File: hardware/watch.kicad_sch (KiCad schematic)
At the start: 30 parts, among them J1 DEBUG, J2 RTC_CALIB, J3 RST, Q1 BC846, SW1 MODE, SW2 ALARM, SW3 LIGHT, U1 STM32L053C8Ux, U2 LCD, Y1 32.768kHz

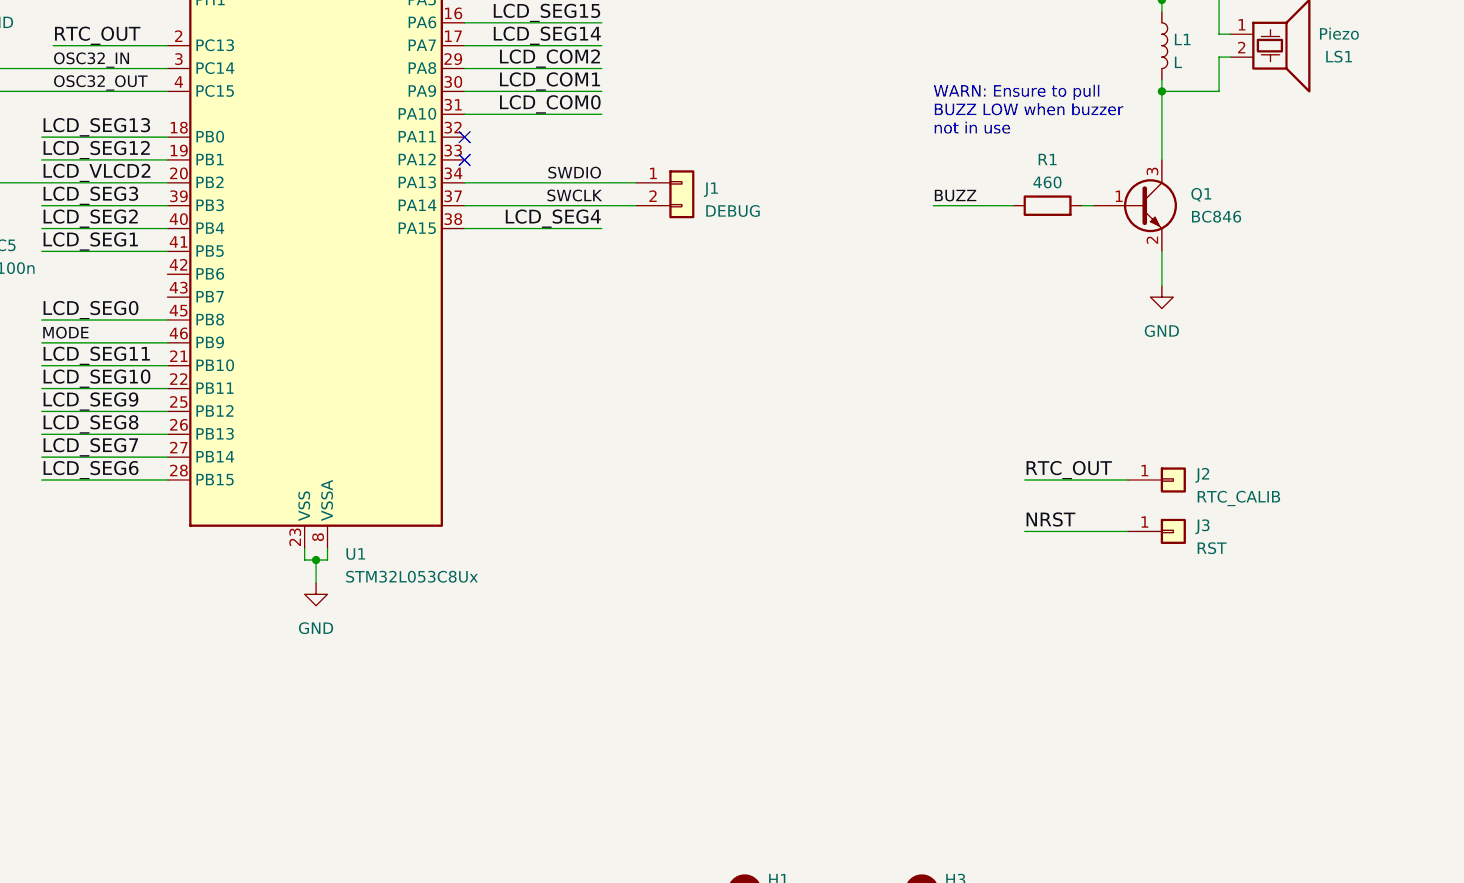
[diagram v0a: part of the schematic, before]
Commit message: Use Paw Connect for debug connector
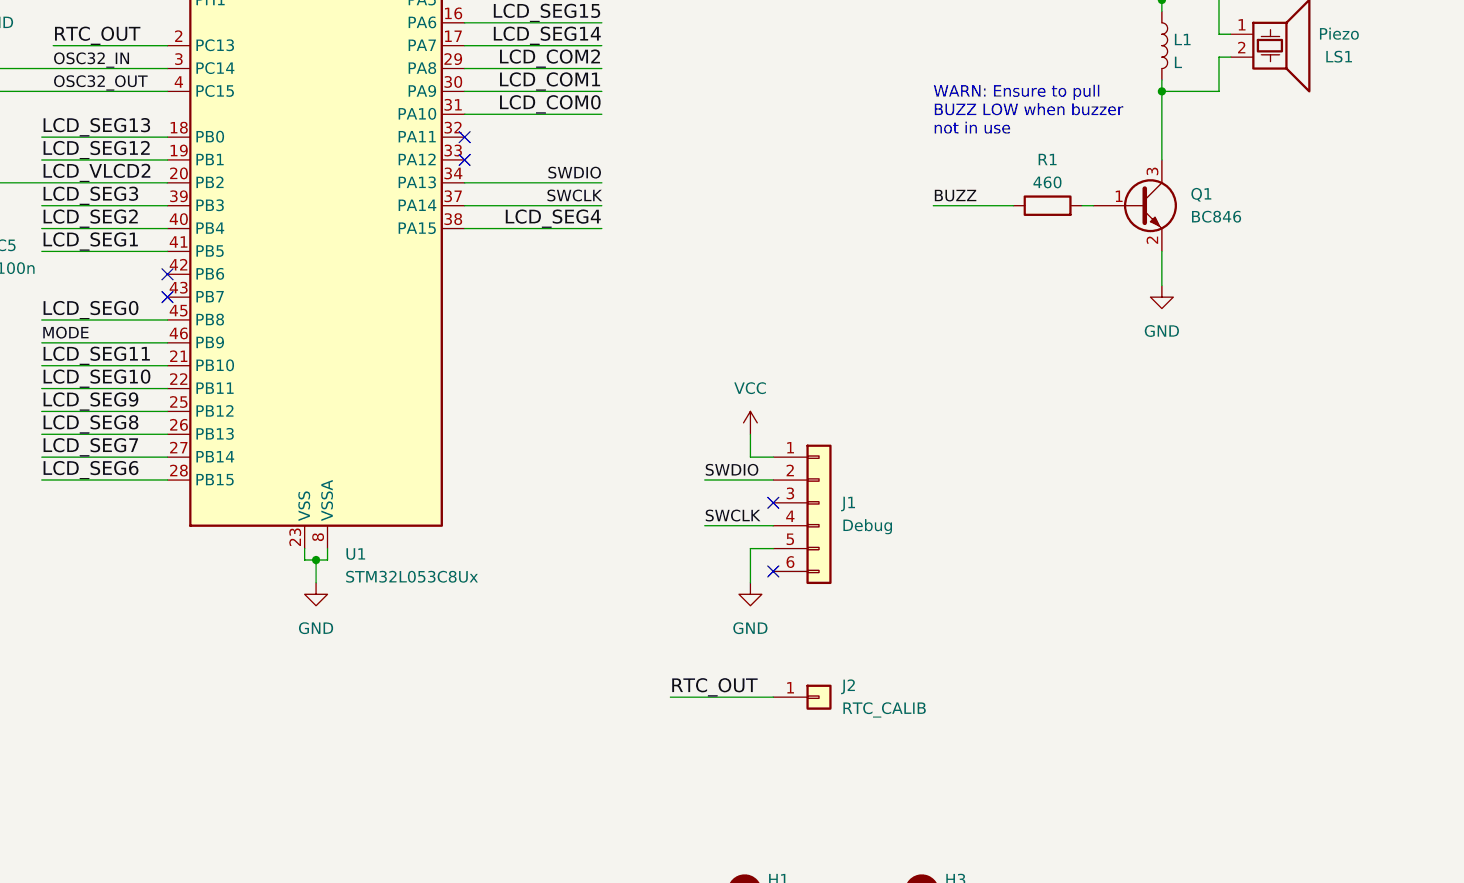
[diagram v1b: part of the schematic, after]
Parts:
- removed J1: DEBUG, Jumper:SolderJumper-2_P1.3mm_Open_Pad1.0x1.5mm, symbol Connector_Generic:Conn_01x02
- removed J3: RST, TestPoint:TestPoint_Pad_1.0x1.0mm, symbol Connector_Generic:Conn_01x01
- added J1: Debug, Paw-Connect:Paw-Connect_RevB_TC2030-IDC-NL_2x03_P1.27mm_Vertical, symbol Connector_Generic:Conn_01x06
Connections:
- net GND: now also J1.5 (Pin_5)
- net SWCLK: now also J1.4 (Pin_4)
- net SWDIO: now also J1.2 (Pin_2)
- net VCC: now also J1.1 (Pin_1)
- no-connect marks 2 -> 6
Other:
- moved on the sheet: J2
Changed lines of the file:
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@@
   (junction (at 38.1 102.87) (diameter 0) (color 0 0 0 0)
   )
+  (no_connect (at 143.51 149.86))
+  (no_connect (at 76.2 116.84))
+  (no_connect (at 143.51 142.24))
+  (no_connect (at 76.2 119.38))
   (no_connect (at 109.22 101.6))
   (no_connect (at 109.22 104.14))
@@
     (stroke (width 0) (type default))
   )
-  (wire (pts (xy 109.22 106.68) (xy 128.27 106.68))
+  (wire (pts (xy 109.22 106.68) (xy 124.46 106.68))
     (stroke (width 0) (type default))
   )
@@
     (stroke (width 0) (type default))
   )
+  (wire (pts (xy 135.89 144.78) (xy 143.51 144.78))
+    (stroke (width 0) (type default))
+  )
   (wire (pts (xy 78.74 48.26) (xy 78.74 49.53))
     (stroke (width 0) (type default))
   )
+  (wire (pts (xy 140.97 137.16) (xy 143.51 137.16))
+    (stroke (width 0) (type default))
+  )
   (wire (pts (xy 205.74 41.91) (xy 205.74 57.15))
     (stroke (width 0) (type default))
@@
     (stroke (width 0) (type default))
   )
-  (wire (pts (xy 109.22 109.22) (xy 128.27 109.22))
+  (wire (pts (xy 109.22 109.22) (xy 124.46 109.22))
     (stroke (width 0) (type default))
   )
@@
     (stroke (width 0) (type default))
   )
+  (wire (pts (xy 135.89 139.7) (xy 143.51 139.7))
+    (stroke (width 0) (type default))
+  )
   (wire (pts (xy 193.04 90.17) (xy 193.04 86.36))
     (stroke (width 0) (type default))
@@
     (stroke (width 0) (type default))
   )
+  (wire (pts (xy 143.51 147.32) (xy 140.97 147.32))
+    (stroke (width 0) (type default))
+  )
   (wire (pts (xy 67.31 57.15) (xy 67.31 58.42))
     (stroke (width 0) (type default))
   )
-  (wire (pts (xy 171.45 139.7) (xy 182.88 139.7))
+  (wire (pts (xy 132.08 163.83) (xy 143.51 163.83))
     (stroke (width 0) (type default))
   )
@@
     (stroke (width 0) (type default))
   )
-  (wire (pts (xy 171.45 145.415) (xy 182.88 145.415))
-    (stroke (width 0) (type default))
-  )
   (wire (pts (xy 264.16 118.11) (xy 269.24 118.11))
     (stroke (width 0) (type default))
@@
     (stroke (width 0) (type default))
   )
+  (wire (pts (xy 140.97 134.62) (xy 140.97 137.16))
+    (stroke (width 0) (type default))
+  )
   (wire (pts (xy 93.98 148.59) (xy 92.71 148.59))
     (stroke (width 0) (type default))
@@
   )
   (wire (pts (xy 22.86 185.42) (xy 22.86 186.69))
+    (stroke (width 0) (type default))
+  )
+  (wire (pts (xy 140.97 147.32) (xy 140.97 151.13))
     (stroke (width 0) (type default))
   )
@@
     (effects (font (size 1.524 1.524)) (justify left bottom))
   )
+  (label "SWDIO" (at 135.89 139.7 0) (fields_autoplaced)
+    (effects (font (size 1.27 1.27)) (justify left bottom))
+  )
   (label "LCD_SEG3" (at 62.23 109.22 0) (fields_autoplaced)
     (effects (font (size 1.524 1.524)) (justify left bottom))
@@
     (effects (font (size 1.524 1.524)) (justify right bottom))
   )
-  (label "RTC_OUT" (at 171.45 139.7 0) (fields_autoplaced)
+  (label "RTC_OUT" (at 132.08 163.83 0) (fields_autoplaced)
     (effects (font (size 1.524 1.524)) (justify left bottom))
   )
@@
     (effects (font (size 1.524 1.524)) (justify left bottom))
   )
+  (label "SWCLK" (at 135.89 144.78 0) (fields_autoplaced)
+    (effects (font (size 1.27 1.27)) (justify left bottom))
+  )
   (label "LCD_SEG6" (at 62.23 139.7 0) (fields_autoplaced)
     (effects (font (size 1.524 1.524)) (justify left bottom))
@@
     (effects (font (size 1.524 1.524)) (justify right bottom))
   )
-  (label "NRST" (at 171.45 145.415 0) (fields_autoplaced)
-    (effects (font (size 1.524 1.524)) (justify left bottom))
-  )
   (label "LCD_SEG10" (at 259.08 57.15 90) (fields_autoplaced)
     (effects (font (size 1.524 1.524)) (justify left bottom))
@@
     )
   )
-  (symbol (lib_id "Connector_Generic:Conn_01x01") (at 187.96 139.7 0) (unit 1)
-    (in_bom yes) (on_board yes) (dnp no) (fields_autoplaced)
-    (property "Reference" "J2" (at 190.5 139.065 0)
-      (effects (font (size 1.27 1.27)) (justify left))
-    )
-    (property "Value" "RTC_CALIB" (at 190.5 141.605 0)
-      (effects (font (size 1.27 1.27)) (justify left))
-    )
-    (property "Footprint" "TestPoint:TestPoint_Pad_1.0x1.0mm" (at 187.96 139.7 0)
-      (effects (font (size 1.27 1.27)) hide)
-    )
-    (property "Datasheet" "~" (at 187.96 139.7 0)
+  (symbol (lib_id "Connector_Generic:Conn_01x01") (at 148.59 163.83 0) (unit 1)
+    (in_bom yes) (on_board yes) (dnp no) (fields_autoplaced)
+    (property "Reference" "J2" (at 151.13 162.56 0)
+      (effects (font (size 1.27 1.27)) (justify left))
+    )
+    (property "Value" "RTC_CALIB" (at 151.13 165.1 0)
+      (effects (font (size 1.27 1.27)) (justify left))
+    )
+    (property "Footprint" "TestPoint:TestPoint_Pad_1.0x1.0mm" (at 148.59 163.83 0)
+      (effects (font (size 1.27 1.27)) hide)
+    )
+    (property "Datasheet" "~" (at 148.59 163.83 0)
       (effects (font (size 1.27 1.27)) hide)
     )
@@
     )
   )
+  (symbol (lib_id "power:VCC") (at 140.97 134.62 0) (unit 1)
+    (in_bom yes) (on_board yes) (dnp no) (fields_autoplaced)
+    (property "Reference" "#PWR012" (at 140.97 138.43 0)
+      (effects (font (size 1.27 1.27)) hide)
+    )
+    (property "Value" "VCC" (at 140.97 129.54 0)
+      (effects (font (size 1.27 1.27)))
+    )
+    (property "Footprint" "" (at 140.97 134.62 0)
+      (effects (font (size 1.27 1.27)) hide)
+    )
+    (property "Datasheet" "" (at 140.97 134.62 0)
+      (effects (font (size 1.27 1.27)) hide)
+    )
+    (pin "1")
+    (instances
+      (project "watch"
+        (path "/1b31cf37-5c4a-4947-b9a5-75d98c6c2434"
+          (reference "#PWR012") (unit 1)
+        )
+      )
+    )
+  )
   (symbol (lib_id "Device:L") (at 186.69 91.44 0) (unit 1)
     (in_bom yes) (on_board yes) (dnp no) (fields_autoplaced)
@@
         (path "/1b31cf37-5c4a-4947-b9a5-75d98c6c2434"
           (reference "#PWR09") (unit 1)
+        )
+      )
+    )
+  )
+  (symbol (lib_name "GND_3") (lib_id "power:GND") (at 140.97 151.13 0) (unit 1)
+    (in_bom yes) (on_board yes) (dnp no) (fields_autoplaced)
+    (property "Reference" "#PWR08" (at 140.97 157.48 0)
+      (effects (font (size 1.27 1.27)) hide)
+    )
+    (property "Value" "GND" (at 140.97 156.21 0)
+      (effects (font (size 1.27 1.27)))
+    )
+    (property "Footprint" "" (at 140.97 151.13 0)
+      (effects (font (size 1.27 1.27)) hide)
+    )
+    (property "Datasheet" "" (at 140.97 151.13 0)
+      (effects (font (size 1.27 1.27)) hide)
+    )
+    (pin "1")
+    (instances
+      (project "watch"
+        (path "/1b31cf37-5c4a-4947-b9a5-75d98c6c2434"
+          (reference "#PWR08") (unit 1)
         )
       )
@@
     )
   )
-  (symbol (lib_id "Connector_Generic:Conn_01x01") (at 187.96 145.415 0) (unit 1)
-    (in_bom yes) (on_board yes) (dnp no) (fields_autoplaced)
-    (property "Reference" "J3" (at 190.5 144.78 0)
-      (effects (font (size 1.27 1.27)) (justify left))
-    )
-    (property "Value" "RST" (at 190.5 147.32 0)
-      (effects (font (size 1.27 1.27)) (justify left))
-    )
-    (property "Footprint" "TestPoint:TestPoint_Pad_1.0x1.0mm" (at 187.96 145.415 0)
-      (effects (font (size 1.27 1.27)) hide)
-    )
-    (property "Datasheet" "~" (at 187.96 145.415 0)
-      (effects (font (size 1.27 1.27)) hide)
-    )
-    (pin "1")
-    (instances
-      (project "watch"
-        (path "/1b31cf37-5c4a-4947-b9a5-75d98c6c2434"
-          (reference "J3") (unit 1)
-        )
-      )
-    )
-  )
   (symbol (lib_id "Device:C") (at 55.88 53.34 0) (unit 1)
     (in_bom yes) (on_board yes) (dnp no) (fields_autoplaced)
@@
     )
   )
+  (symbol (lib_id "Connector_Generic:Conn_01x06") (at 148.59 142.24 0) (unit 1)
+    (in_bom yes) (on_board yes) (dnp no) (fields_autoplaced)
+    (property "Reference" "J1" (at 151.13 142.24 0)
+      (effects (font (size 1.27 1.27)) (justify left))
+    )
+    (property "Value" "Debug" (at 151.13 144.78 0)
+      (effects (font (size 1.27 1.27)) (justify left))
+    )
+    (property "Footprint" "Paw-Connect:Paw-Connect_RevB_TC2030-IDC-NL_2x03_P1.27mm_Vertical" (at 148.59 142.24 0)
+      (effects (font (size 1.27 1.27)) hide)
+    )
+    (property "Datasheet" "~" (at 148.59 142.24 0)
+      (effects (font (size 1.27 1.27)) hide)
+    )
+    (pin "1")
+    (pin "2")
+    (pin "5")
+    (pin "3")
+    (pin "4")
+    (pin "6")
+    (instances
+      (project "watch"
+        (path "/1b31cf37-5c4a-4947-b9a5-75d98c6c2434"
+          (reference "J1") (unit 1)
+        )
+      )
+    )
+  )
   (symbol (lib_id "Device:Crystal") (at 31.75 102.87 0) (mirror x) (unit 1)
     (in_bom yes) (on_board yes) (dnp no) (fields_autoplaced)
@@
         )
       )
-    )
-  )
-  (symbol (lib_id "Connector_Generic:Conn_01x02") (at 133.35 106.68 0) (unit 1)
-    (in_bom yes) (on_board yes) (dnp no) (fields_autoplaced)
-    (property "Reference" "J1" (at 135.89 107.315 0)
-      (effects (font (size 1.27 1.27)) (justify left))
-    )
-    (property "Value" "DEBUG" (at 135.89 109.855 0)
-      (effects (font (size 1.27 1.27)) (justify left))
-    )
-    (property "Footprint" "Jumper:SolderJumper-2_P1.3mm_Open_Pad1.0x1.5mm" (at 133.35 106.68 0)
-      (effects (font (size 1.27 1.27)) hide)
-    )
-    (property "Datasheet" "~" (at 133.35 106.68 0)
-      (effects (font (size 1.27 1.27)) hide)
-    )
-    (pin "1")
-    (pin "2")
-    (instances
-      (project "watch"
-        (path "/1b31cf37-5c4a-4947-b9a5-75d98c6c2434"
-          (reference "J1") (unit 1)
-        )
-      )

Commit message: Update footprint library name
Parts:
- LS1: footprint f-91w:Buzzer -> Watch:Buzzer
- U2: footprint f-91w:LCD -> Watch:LCD
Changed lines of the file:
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@@
       (effects (font (size 1.524 1.524)))
     )
-    (property "Footprint" "f-91w:LCD" (at 236.22 29.21 0)
+    (property "Footprint" "Watch:LCD" (at 236.22 29.21 0)
       (effects (font (size 1.524 1.524)) hide)
     )
@@
       (effects (font (size 1.27 1.27)))
     )
-    (property "Footprint" "f-91w:Buzzer" (at 198.501 91.44 0)
-      (effects (font (size 1.27 1.27)) hide)
-    )
+    (property "Footprint" "Watch:Buzzer" (at 198.501 91.44 0)
+      (effects (font (size 1.27 1.27)) hide)
+    )
